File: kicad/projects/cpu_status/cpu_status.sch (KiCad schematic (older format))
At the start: 108 parts, among them J1 Control_signal_backplane, J2 Aux_connection, J3 Bus_connection, J4 MAR_content_in, J5 Conn_01x03_Male, J6 Conn_01x02_Female, U1 74HC245, U10 74HC04, U2 74HC245, U3 74HC245, U4 74HC245, U5 74HC245, U6 74HC245, U7 74HC245, U8 74HC245, U9 74HC126

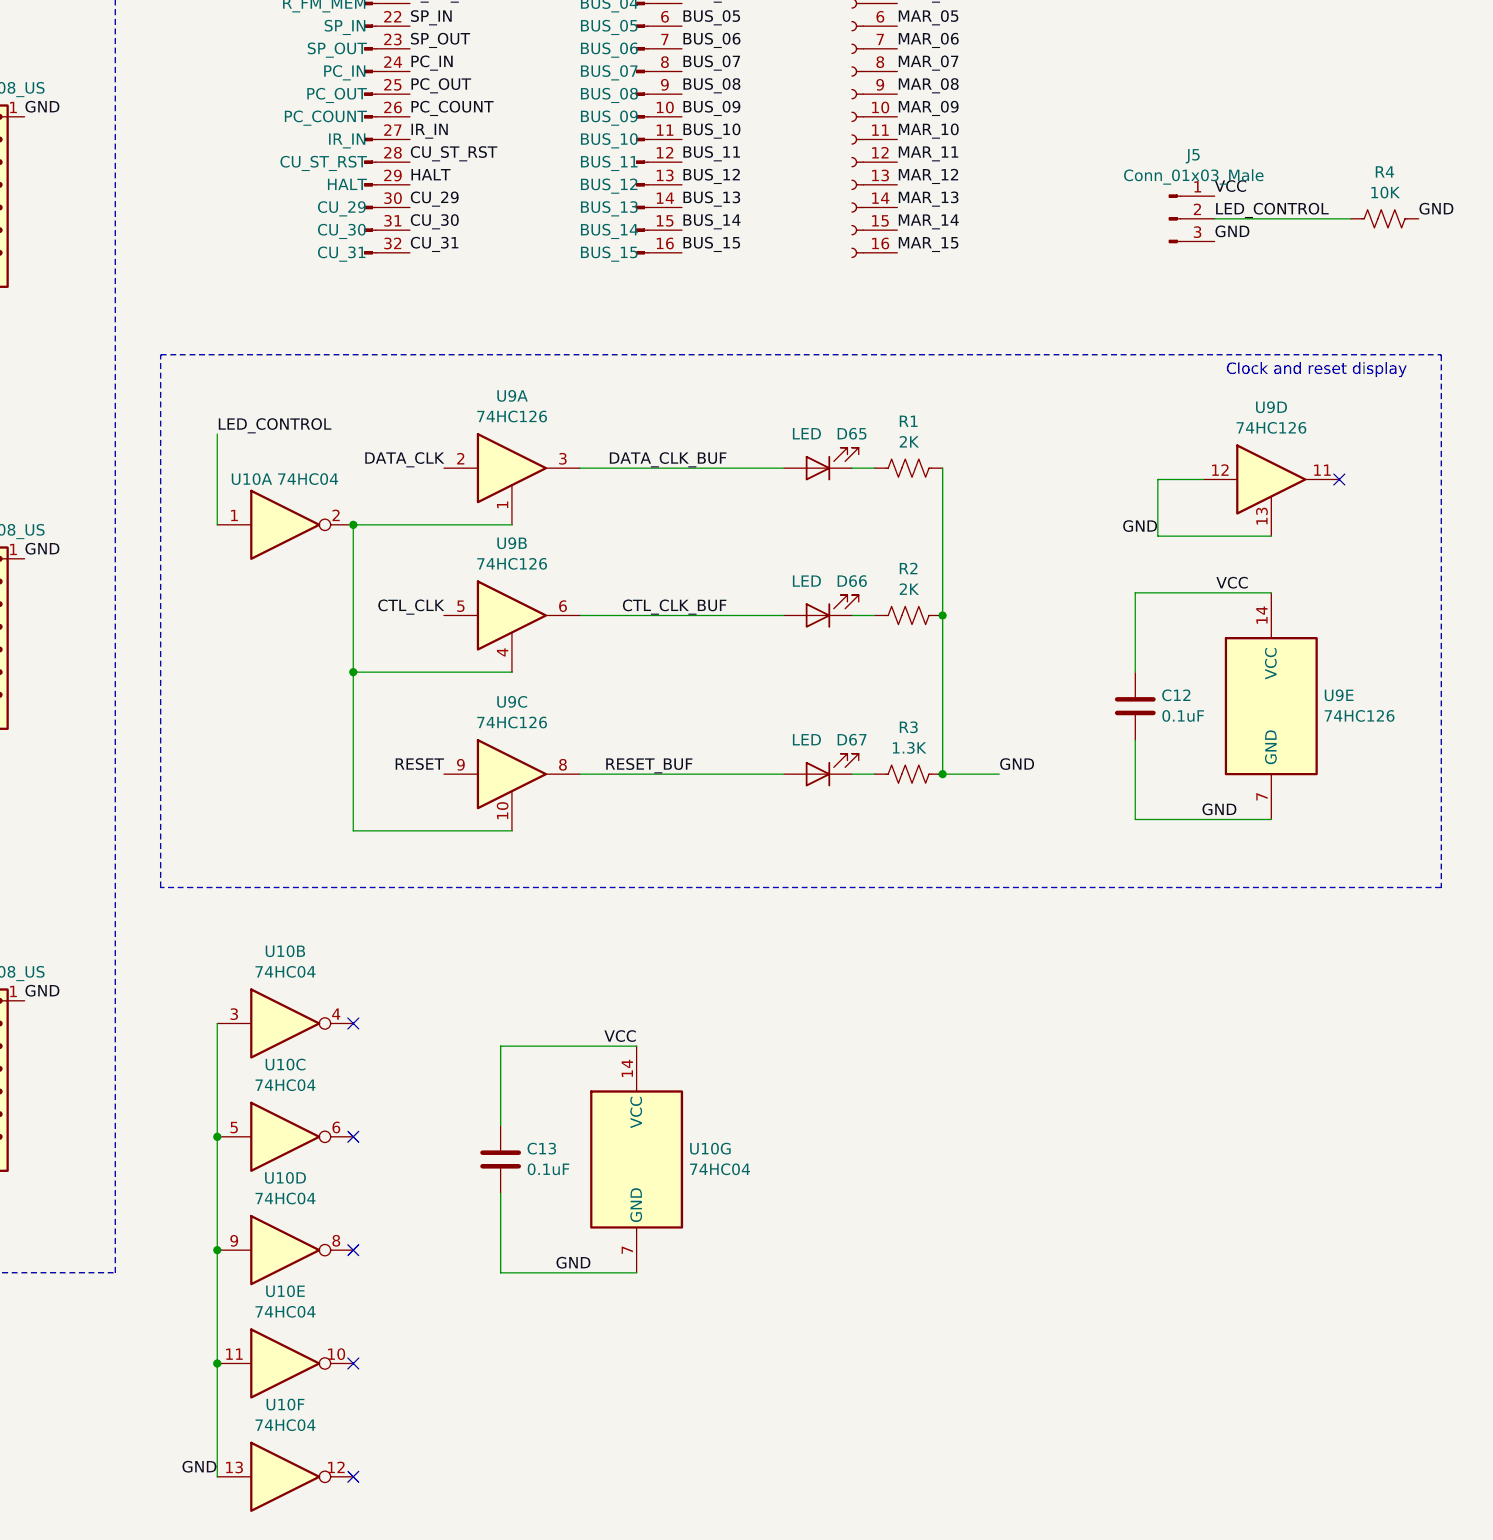
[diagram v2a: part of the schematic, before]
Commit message: Part way through adding ECNZ to status.
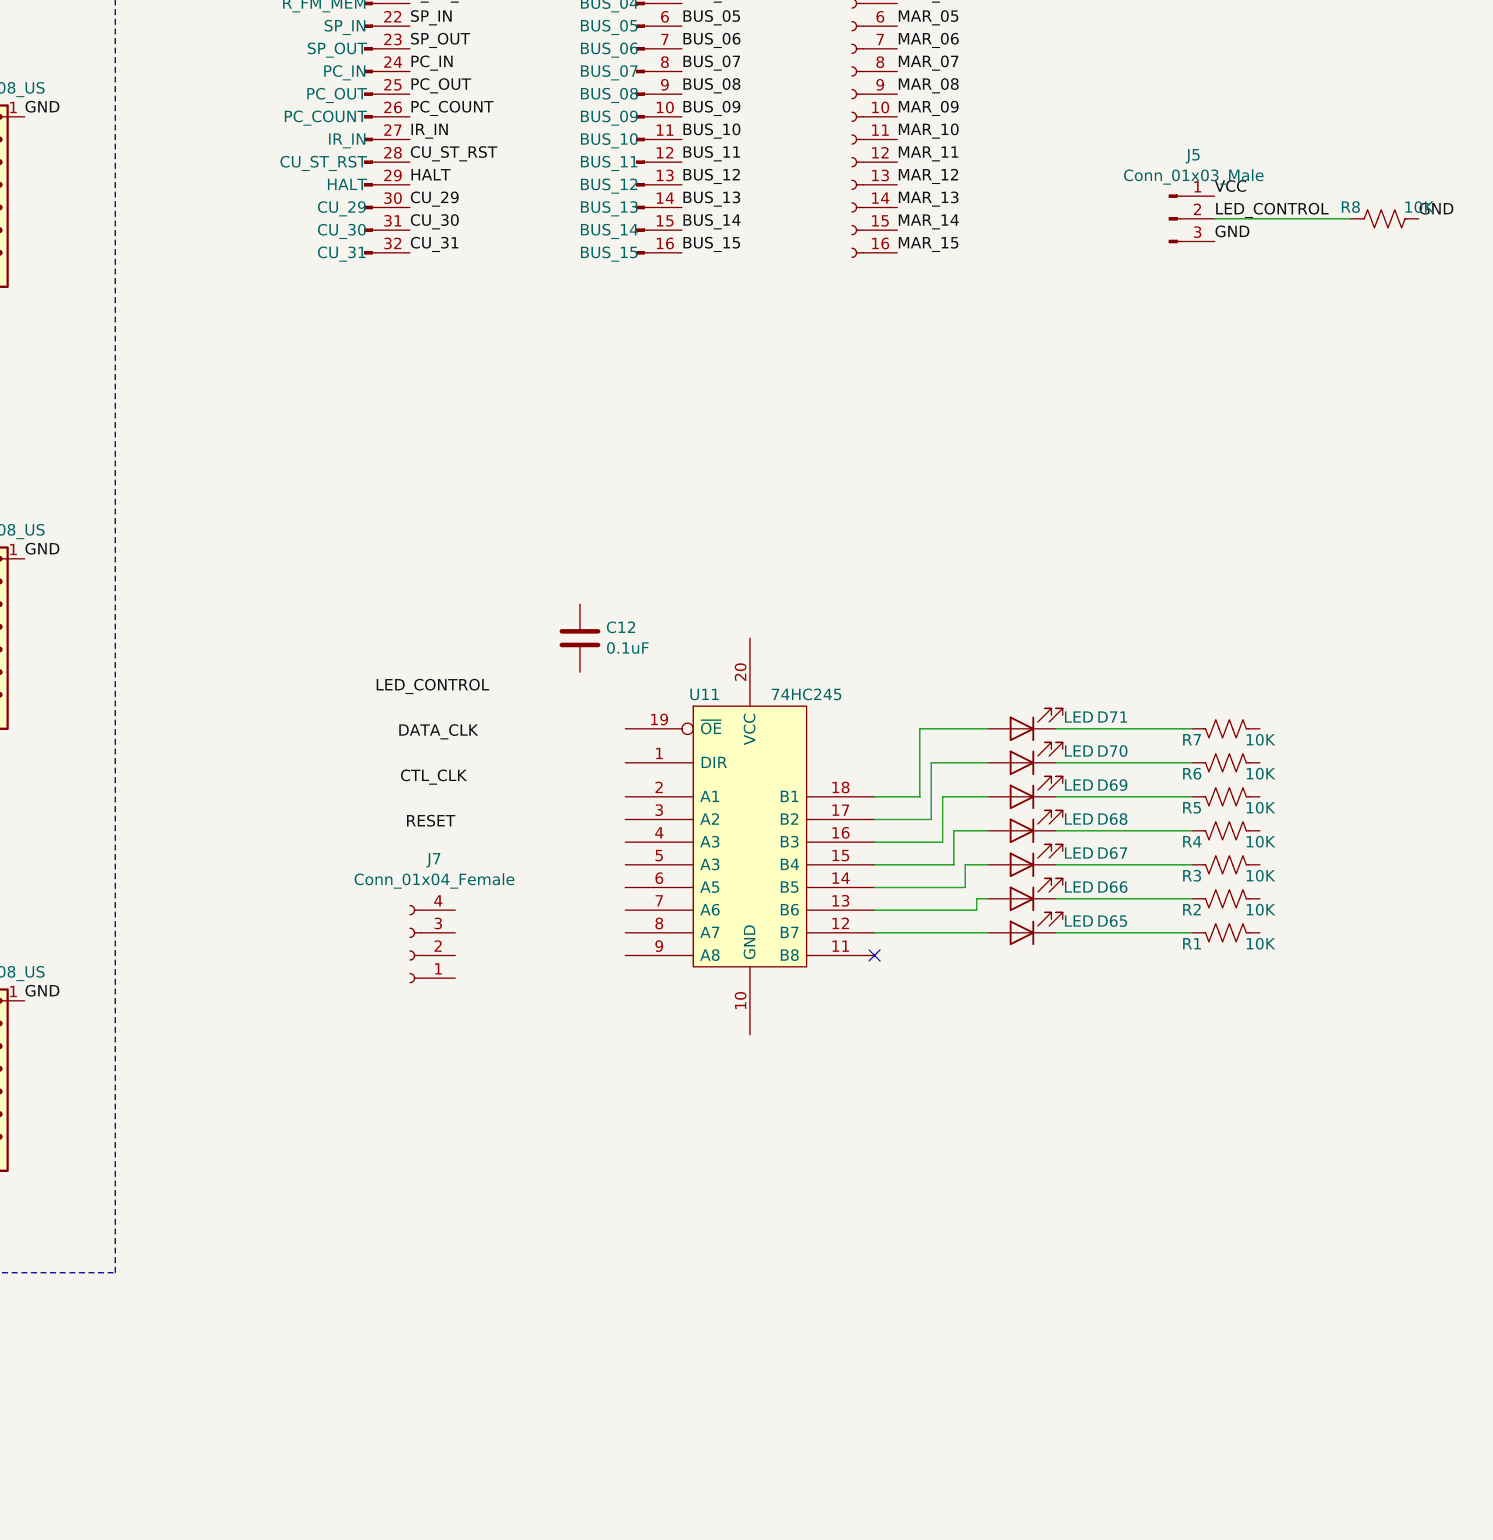
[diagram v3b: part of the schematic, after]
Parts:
- removed C13: 0.1uF, Capacitor_THT:C_Disc_D4.7mm_W2.5mm_P5.00mm, symbol Device:C
- removed U10: 74HC04, Package_DIP:DIP-14_W7.62mm, symbol 74xx:74HC04
- removed U9: 74HC126, Package_DIP:DIP-14_W7.62mm, symbol sixteen-bit-computer:74HC126
- added D68, D69, D70, D71: LED, sixteen-bit-computer:LED_D5.0mm, symbol Device:LED
- added J7: Conn_01x04_Female, Connector_PinSocket_2.54mm:PinSocket_1x04_P2.54mm_Horizontal, symbol Connector:Conn_01x04_Female
- added R5, R6, R7: 10K, Resistor_THT:R_Axial_DIN0207_L6.3mm_D2.5mm_P2.54mm_Vertical, symbol Device:R_US
- added R8: 10K, Resistor_THT:R_Axial_DIN0207_L6.3mm_D2.5mm_P10.16mm_Horizontal, symbol Device:R_US
- added U11: 74HC245, Package_DIP:DIP-20_W7.62mm, symbol sixteen-bit-computer:74HC245
- R1, R2: value 2K -> 10K; footprint Resistor_THT:R_Axial_DIN0207_L6.3mm_D2.5mm_P10.16mm_Horizontal -> Resistor_THT:R_Axial_DIN0207_L6.3mm_D2.5mm_P2.54mm_Vertical
- R3: value 1.3K -> 10K; footprint Resistor_THT:R_Axial_DIN0207_L6.3mm_D2.5mm_P10.16mm_Horizontal -> Resistor_THT:R_Axial_DIN0207_L6.3mm_D2.5mm_P2.54mm_Vertical
- R4: footprint Resistor_THT:R_Axial_DIN0207_L6.3mm_D2.5mm_P10.16mm_Horizontal -> Resistor_THT:R_Axial_DIN0207_L6.3mm_D2.5mm_P2.54mm_Vertical
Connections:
- net GND: now also R8.1; no longer C12.2, R1.1, R2.1, R3.1, R4.1
- net LED_CONTROL: now also R8.2; no longer R4.2
- net VCC: no longer C12.1
- net CTL_CLK_BUF: no longer names the net of D66.2 (A)
- net CTL_CLK_BUF: now also U11.13 (B6)
- net DATA_CLK_BUF: no longer names the net of D65.2 (A)
- net DATA_CLK_BUF: now also U11.12 (B7)
- net RESET_BUF: no longer names the net of D67.2 (A)
- net RESET_BUF: now also U11.14 (B5)
- new net: D68.1 (K), R4.2
- new net: D68.2 (A), U11.15 (B4)
- new net: D69.2 (A), U11.16 (B3)
- new net: D70.2 (A), U11.17 (B2)
- new net: D71.2 (A), U11.18 (B1)
- new net: D69.1 (K), R5.2
- new net: D70.1 (K), R6.2
- new net: D71.1 (K), R7.2
- no-connect marks 6 -> 1
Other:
- note removed: "Clock and reset display"
- moved on the sheet: R4
